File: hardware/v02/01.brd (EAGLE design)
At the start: 91.1 x 43.8 mm, 31 parts, among them IC1 MSP430G2553, IC2 78L05Z, X2 RJ45-6L-B

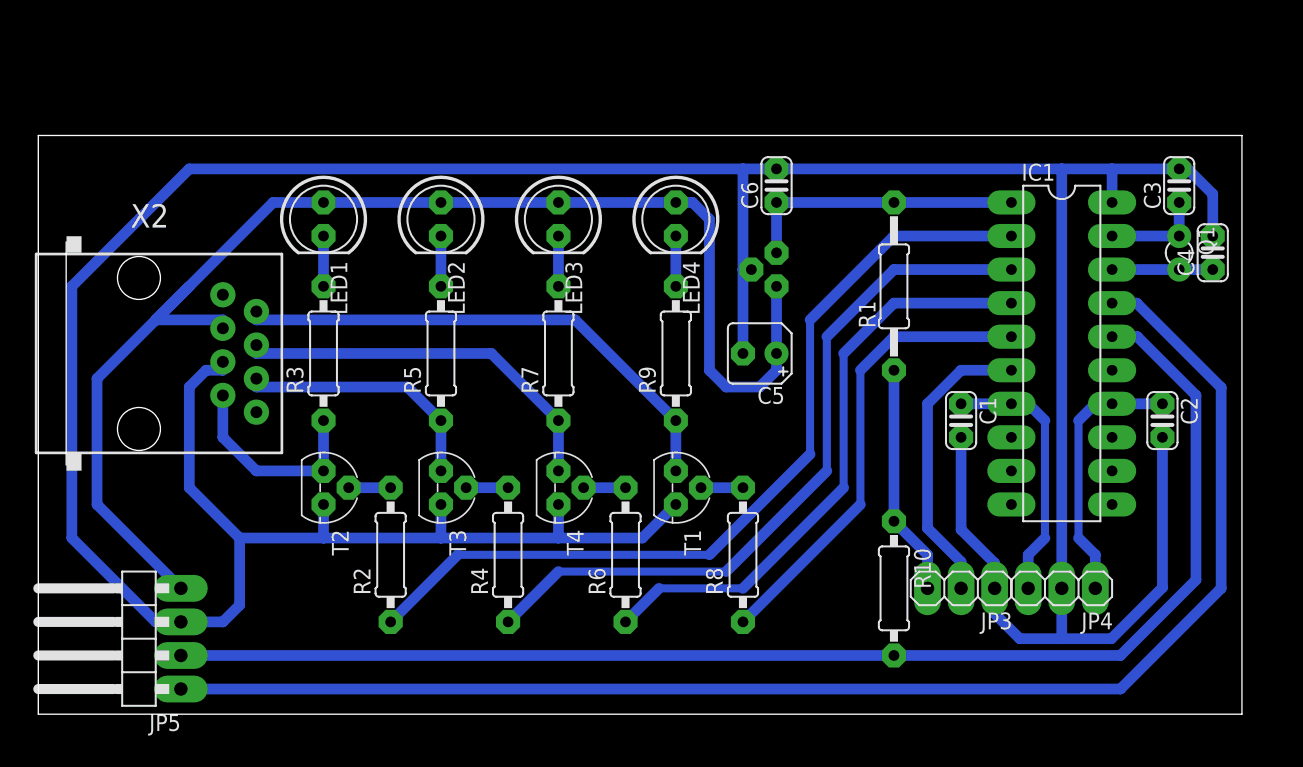
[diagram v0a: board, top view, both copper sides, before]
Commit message: XTAl flat on board; holes for additional wire
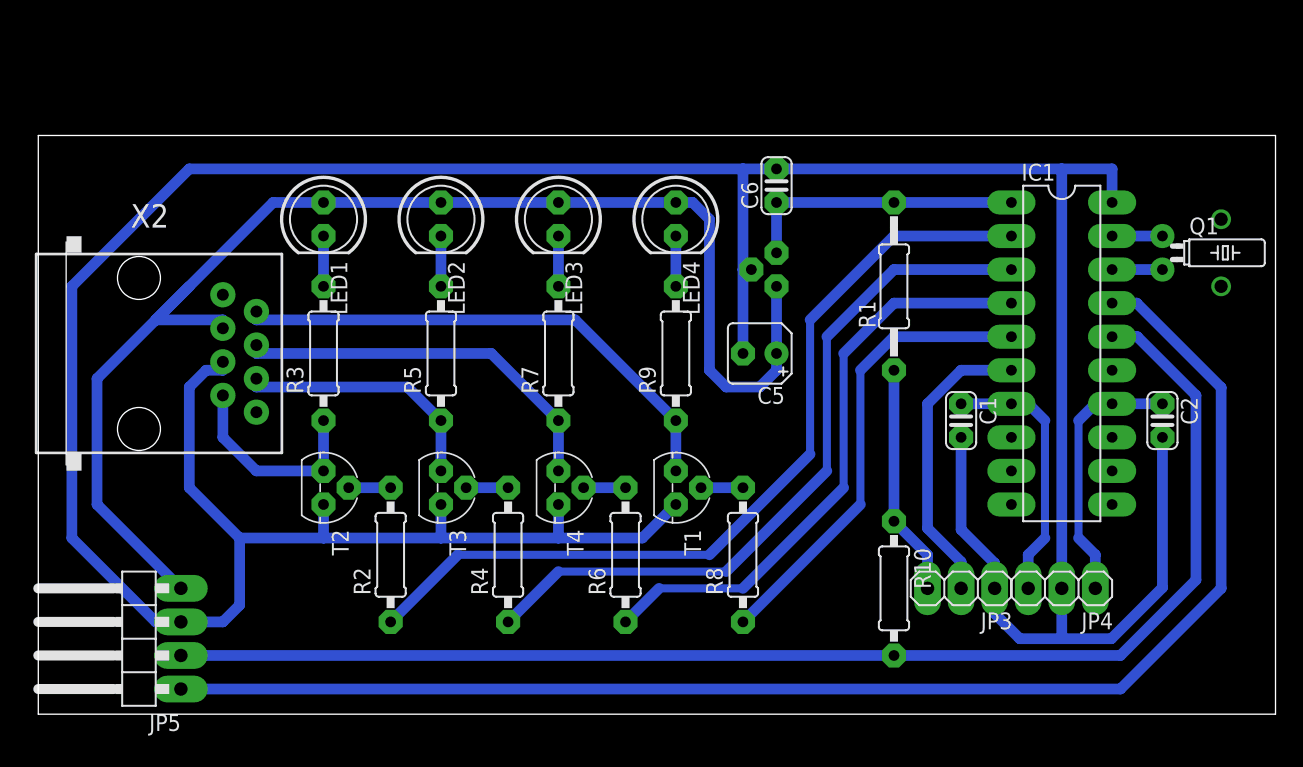
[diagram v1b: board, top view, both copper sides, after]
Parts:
- removed C3, C4: 12pF, rcl:C025-024X044
- Q1: device crystal:TC26V -> crystal:TC26H
- moved Q1 1.27 mm to (85.1, 34.9)
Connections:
- net GND: no longer C3.2, C4.2
- net N$2: no longer C3.1
- net N$7: no longer C4.1
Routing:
- net GND: track 286.0 -> 274.4 mm
- net N$7: track 7.62 -> 3.81 mm
- net N$2: track 7.62 -> 3.81 mm
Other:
- board size 91.1 x 43.8 mm -> 93.7 x 43.8 mm
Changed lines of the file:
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@@
 <board>
 <plain>
-<wire x1="0" y1="0" x2="91.11" y2="0" width="0" layer="20"/>
-<wire x1="91.11" y1="0" x2="91.11" y2="43.805" width="0" layer="20"/>
-<wire x1="91.11" y1="43.805" x2="0" y2="43.805" width="0" layer="20"/>
+<wire x1="0" y1="0" x2="93.65" y2="0" width="0" layer="20"/>
+<wire x1="93.65" y1="0" x2="93.65" y2="43.805" width="0" layer="20"/>
+<wire x1="93.65" y1="43.805" x2="0" y2="43.805" width="0" layer="20"/>
 <wire x1="0" y1="43.805" x2="0" y2="0" width="0" layer="20"/>
 </plain>
@@
 <element name="C1" library="rcl" package="C025-024X044" value="100nF" x="69.85" y="22.225" rot="R270"/>
 <element name="C2" library="rcl" package="C025-024X044" value="100nF" x="85.09" y="22.225" rot="R270"/>
-<element name="Q1" library="crystal" package="TC26V" value="" x="86.36" y="34.925" rot="R270">
-<attribute name="MF" value="" x="86.36" y="34.925" size="1.778" layer="27" rot="R270" display="off"/>
-<attribute name="MPN" value="" x="86.36" y="34.925" size="1.778" layer="27" rot="R270" display="off"/>
-<attribute name="OC_FARNELL" value="unknown" x="86.36" y="34.925" size="1.778" layer="27" rot="R270" display="off"/>
-<attribute name="OC_NEWARK" value="unknown" x="86.36" y="34.925" size="1.778" layer="27" rot="R270" display="off"/>
+<element name="Q1" library="crystal" package="TC26H" value="" x="85.09" y="34.925" rot="R270">
+<attribute name="MF" value="" x="85.09" y="34.925" size="1.778" layer="27" rot="R270" display="off"/>
+<attribute name="MPN" value="" x="85.09" y="34.925" size="1.778" layer="27" rot="R270" display="off"/>
+<attribute name="OC_FARNELL" value="unknown" x="85.09" y="34.925" size="1.778" layer="27" rot="R270" display="off"/>
+<attribute name="OC_NEWARK" value="unknown" x="85.09" y="34.925" size="1.778" layer="27" rot="R270" display="off"/>
 </element>
-<element name="C3" library="rcl" package="C025-024X044" value="12pF" x="86.36" y="40.005" rot="R90"/>
 <element name="R8" library="rcl" package="0207/10" value="470" x="53.34" y="12.065" rot="R90"/>
 <element name="R9" library="rcl" package="0207/10" value="220" x="48.26" y="27.305" rot="R90"/>
@@
 <attribute name="OC_NEWARK" value="16R6090" x="7.62" y="27.305" size="1.778" layer="27" rot="R270" display="off"/>
 </element>
-<element name="C4" library="rcl" package="C025-024X044" value="12pF" x="88.9" y="34.925" rot="R90"/>
 <element name="R1" library="rcl" package="0207/12" value="0" x="64.77" y="32.385" rot="R90"/>
 <element name="R10" library="rcl" package="0207/10" value="47k" x="64.77" y="9.525" rot="R270"/>
@@
 <contactref element="C2" pad="2"/>
 <contactref element="IC1" pad="20"/>
-<contactref element="C3" pad="2"/>
 <contactref element="IC2" pad="2"/>
 <contactref element="C5" pad="-"/>
@@
 <contactref element="X2" pad="5"/>
 <contactref element="JP5" pad="3"/>
-<contactref element="C4" pad="2"/>
 <wire x1="21.59" y1="13.335" x2="21.59" y2="15.875" width="0.8128" layer="16"/>
 <wire x1="21.59" y1="13.335" x2="30.48" y2="13.335" width="0.8128" layer="16"/>
@@
 <wire x1="8.89" y1="6.985" x2="10.795" y2="6.985" width="0.8128" layer="16"/>
 <wire x1="81.28" y1="41.275" x2="81.28" y2="38.735" width="0.8128" layer="16"/>
-<wire x1="81.28" y1="41.275" x2="86.36" y2="41.275" width="0.8128" layer="16"/>
-<wire x1="86.36" y1="41.275" x2="86.995" y2="41.275" width="0.8128" layer="16"/>
-<wire x1="86.995" y1="41.275" x2="88.9" y2="39.37" width="0.8128" layer="16"/>
-<wire x1="88.9" y1="39.37" x2="88.9" y2="36.195" width="0.8128" layer="16"/>
 <wire x1="53.34" y1="33.655" x2="53.975" y2="33.655" width="0.8128" layer="16"/>
 <wire x1="53.34" y1="41.275" x2="53.34" y2="33.655" width="0.8128" layer="16"/>
@@
 </signal>
 <signal name="N$2">
-<contactref element="C3" pad="1"/>
 <contactref element="Q1" pad="1"/>
 <contactref element="IC1" pad="19"/>
-<wire x1="81.28" y1="36.195" x2="86.36" y2="36.195" width="0.8128" layer="16"/>
-<wire x1="86.36" y1="36.195" x2="86.36" y2="38.735" width="0.8128" layer="16"/>
+<wire x1="81.28" y1="36.195" x2="85.09" y2="36.195" width="0.8128" layer="16"/>
 </signal>
 <signal name="N$7">
 <contactref element="Q1" pad="2"/>
 <contactref element="IC1" pad="18"/>
-<contactref element="C4" pad="1"/>
-<wire x1="81.28" y1="33.655" x2="86.36" y2="33.655" width="0.8128" layer="16"/>
-<wire x1="86.36" y1="33.655" x2="88.9" y2="33.655" width="0.8128" layer="16"/>
+<wire x1="81.28" y1="33.655" x2="85.09" y2="33.655" width="0.8128" layer="16"/>
 </signal>
 <signal name="+5V">
@@
 <wire x1="67.31" y1="12.065" x2="67.31" y2="9.525" width="0.8128" layer="16"/>
 </signal>
+<signal name="N$18">
+<via x="89.535" y="37.465" extent="1-16" drill="1" shape="square"/>
+</signal>
+<signal name="N$24">
+<via x="89.535" y="32.385" extent="1-16" drill="1" shape="square"/>
+</signal>
+<signal name="N$25">
+</signal>
+<signal name="N$26">
+</signal>
 </signals>

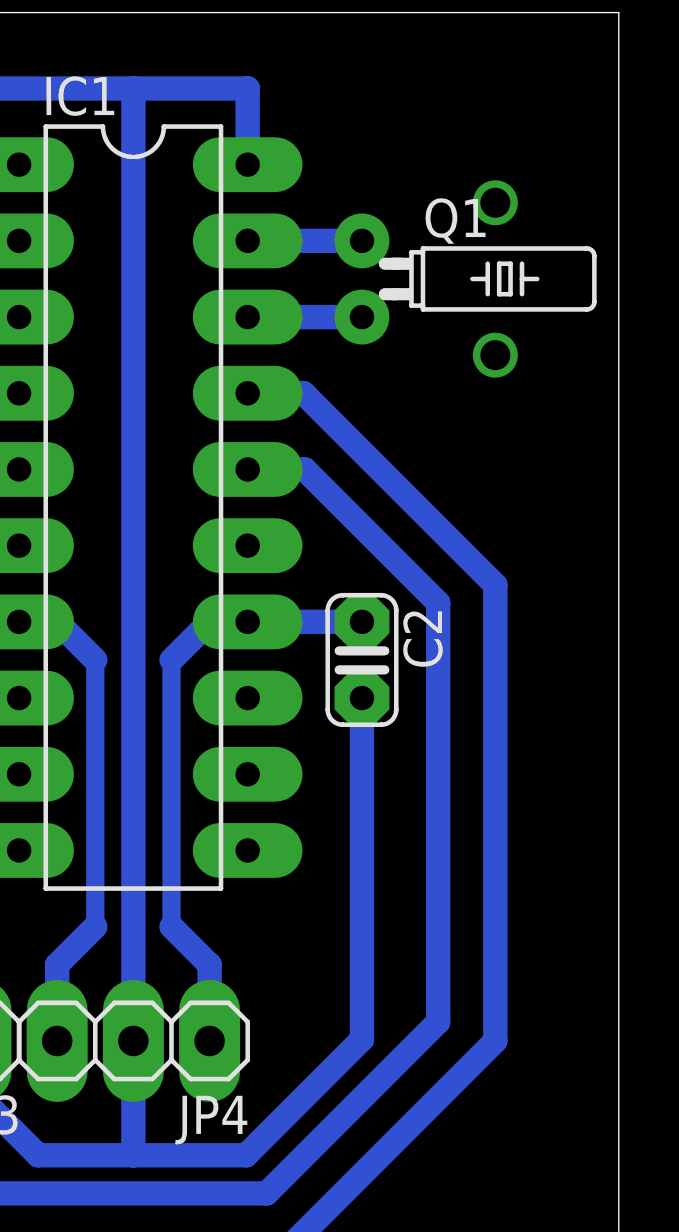
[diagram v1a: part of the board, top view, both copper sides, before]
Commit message: C3 between RST and GND
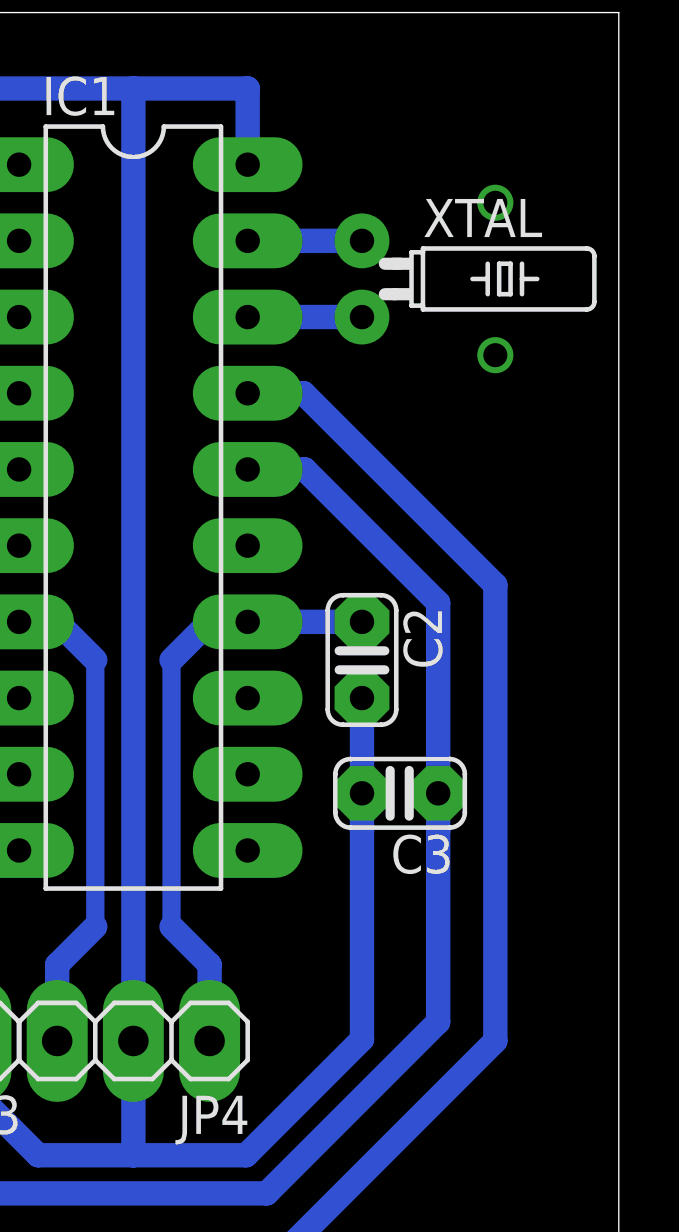
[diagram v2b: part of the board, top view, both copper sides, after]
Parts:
- added C3: 100nF, rcl:C025-024X044
- renumbered Q1 to XTAL
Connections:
- net GND: now also C3.2
- net N$5: now also C3.1
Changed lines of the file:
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@@
 <element name="C1" library="rcl" package="C025-024X044" value="100nF" x="69.85" y="22.225" rot="R270"/>
 <element name="C2" library="rcl" package="C025-024X044" value="100nF" x="85.09" y="22.225" rot="R270"/>
-<element name="Q1" library="crystal" package="TC26H" value="" x="85.09" y="34.925" rot="R270">
+<element name="XTAL" library="crystal" package="TC26H" value="" x="85.09" y="34.925" rot="R270">
 <attribute name="MF" value="" x="85.09" y="34.925" size="1.778" layer="27" rot="R270" display="off"/>
 <attribute name="MPN" value="" x="85.09" y="34.925" size="1.778" layer="27" rot="R270" display="off"/>
@@
 <element name="R1" library="rcl" package="0207/12" value="0" x="64.77" y="32.385" rot="R90"/>
 <element name="R10" library="rcl" package="0207/10" value="47k" x="64.77" y="9.525" rot="R270"/>
+<element name="C3" library="rcl" package="C025-024X044" value="100nF" x="86.36" y="17.78" rot="R180"/>
 </elements>
 <signals>
@@
 <wire x1="77.47" y1="5.715" x2="81.2275" y2="5.715" width="0.8128" layer="16"/>
 <wire x1="81.2275" y1="5.715" x2="85.09" y2="9.5775" width="0.8128" layer="16"/>
-<wire x1="85.09" y1="9.5775" x2="85.09" y2="20.955" width="0.8128" layer="16"/>
+<wire x1="85.09" y1="9.5775" x2="85.09" y2="16.51" width="0.8128" layer="16"/>
+<wire x1="85.09" y1="17.78" x2="85.09" y2="20.955" width="0.8128" layer="16"/>
 <wire x1="53.34" y1="41.275" x2="55.88" y2="41.275" width="0.8128" layer="16"/>
+<contactref element="C3" pad="2"/>
+<wire x1="85.09" y1="17.78" x2="85.09" y2="16.51" width="0.8128" layer="16"/>
 </signal>
 <signal name="N$3">
@@
 <wire x1="64.77" y1="4.445" x2="81.915" y2="4.445" width="0.8128" layer="16"/>
 <wire x1="81.915" y1="4.445" x2="87.63" y2="10.16" width="0.8128" layer="16"/>
-<wire x1="87.63" y1="10.16" x2="87.63" y2="24.13" width="0.8128" layer="16"/>
+<wire x1="87.63" y1="10.16" x2="87.63" y2="16.51" width="0.8128" layer="16"/>
+<wire x1="87.63" y1="17.78" x2="87.63" y2="24.13" width="0.8128" layer="16"/>
 <wire x1="87.63" y1="24.13" x2="83.185" y2="28.575" width="0.8128" layer="16"/>
 <wire x1="83.185" y1="28.575" x2="81.28" y2="28.575" width="0.8128" layer="16"/>
 <contactref element="R10" pad="2"/>
+<contactref element="C3" pad="1"/>
+<wire x1="87.63" y1="17.78" x2="87.63" y2="16.51" width="0.8128" layer="16"/>
 </signal>
 <signal name="N$6">
@@
 </signal>
 <signal name="N$2">
-<contactref element="Q1" pad="1"/>
+<contactref element="XTAL" pad="1"/>
 <contactref element="IC1" pad="19"/>
 <wire x1="81.28" y1="36.195" x2="85.09" y2="36.195" width="0.8128" layer="16"/>
 </signal>
 <signal name="N$7">
-<contactref element="Q1" pad="2"/>
+<contactref element="XTAL" pad="2"/>
 <contactref element="IC1" pad="18"/>
 <wire x1="81.28" y1="33.655" x2="85.09" y2="33.655" width="0.8128" layer="16"/>
@@
 </signal>
 <signal name="N$18">
-<via x="89.535" y="37.465" extent="1-16" drill="1" shape="square"/>
+<via x="89.535" y="37.465" extent="1-16" drill="0.8"/>
 </signal>
 <signal name="N$24">
-<via x="89.535" y="32.385" extent="1-16" drill="1" shape="square"/>
+<via x="89.535" y="32.385" extent="1-16" drill="0.8"/>
 </signal>
 <signal name="N$25">

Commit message: C4 between Vcc and GND
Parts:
- removed C6: 100nF, rcl:C025-024X044
- added C4: 200nF, rcl:B45181A
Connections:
- net GND: now also C4.-; no longer C6.2
- net VCC: now also C4.+; no longer C6.1
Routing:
- net GND: track 274.4 -> 287.7 mm
- net VCC: track 21.6 -> 22.9 mm
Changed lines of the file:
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@@
 <element name="JP4" library="pinhead" package="1X03" value="" x="77.47" y="9.525" rot="R180"/>
 <element name="JP5" library="pinhead" package="1X04/90" value="" x="6.985" y="5.715" rot="R90"/>
-<element name="C6" library="rcl" package="C025-024X044" value="100nF" x="55.88" y="40.005" rot="R90"/>
 <element name="X2" library="con-tycoelectronics" package="RJ45-NO-SHIELD" value="RJ45-6L-B" x="7.62" y="27.305" rot="R270">
 <attribute name="MF" value="" x="7.62" y="27.305" size="1.778" layer="27" rot="R270" display="off"/>
@@
 <element name="R10" library="rcl" package="0207/10" value="47k" x="64.77" y="9.525" rot="R270"/>
 <element name="C3" library="rcl" package="C025-024X044" value="100nF" x="86.36" y="17.78" rot="R180"/>
+<element name="C4" library="rcl" package="B45181A" value="200nF" x="54.61" y="40.005" rot="R180"/>
 </elements>
 <signals>
@@
 <contactref element="IC1" pad="1"/>
 <contactref element="IC2" pad="1"/>
-<contactref element="C6" pad="1"/>
 <contactref element="R1" pad="2"/>
 <wire x1="64.77" y1="38.735" x2="73.66" y2="38.735" width="0.8128" layer="16"/>
-<wire x1="55.88" y1="34.925" x2="55.88" y2="38.735" width="0.8128" layer="16"/>
-<wire x1="55.88" y1="38.735" x2="64.77" y2="38.735" width="0.8128" layer="16"/>
+<contactref element="C4" pad="+"/>
+<wire x1="55.88" y1="40.005" x2="55.88" y2="38.735" width="0.8128" layer="16"/>
+<wire x1="55.88" y1="38.735" x2="55.88" y2="34.925" width="0.8128" layer="16"/>
+<wire x1="64.77" y1="38.735" x2="55.88" y2="38.735" width="0.8128" layer="16"/>
 </signal>
 <signal name="PR">
@@
 <contactref element="JP3" pad="1"/>
 <contactref element="JP4" pad="2"/>
-<contactref element="C6" pad="2"/>
 <contactref element="X2" pad="5"/>
 <contactref element="JP5" pad="3"/>
@@
 <wire x1="13.97" y1="6.985" x2="15.24" y2="8.255" width="0.8128" layer="16"/>
 <wire x1="15.24" y1="8.255" x2="15.24" y2="13.335" width="0.8128" layer="16"/>
-<wire x1="55.88" y1="41.275" x2="77.47" y2="41.275" width="0.8128" layer="16"/>
 <wire x1="77.47" y1="41.275" x2="81.28" y2="41.275" width="0.8128" layer="16"/>
 <wire x1="11.43" y1="41.275" x2="53.34" y2="41.275" width="0.8128" layer="16"/>
@@
 <wire x1="81.28" y1="41.275" x2="81.28" y2="38.735" width="0.8128" layer="16"/>
 <wire x1="53.34" y1="33.655" x2="53.975" y2="33.655" width="0.8128" layer="16"/>
-<wire x1="53.34" y1="41.275" x2="53.34" y2="33.655" width="0.8128" layer="16"/>
+<wire x1="53.34" y1="40.005" x2="53.34" y2="33.655" width="0.8128" layer="16"/>
 <wire x1="53.34" y1="33.655" x2="53.34" y2="27.305" width="0.8128" layer="16"/>
 <wire x1="77.47" y1="41.275" x2="77.47" y2="9.525" width="0.8128" layer="16"/>
@@
 <wire x1="77.47" y1="5.715" x2="81.2275" y2="5.715" width="0.8128" layer="16"/>
 <wire x1="81.2275" y1="5.715" x2="85.09" y2="9.5775" width="0.8128" layer="16"/>
-<wire x1="85.09" y1="9.5775" x2="85.09" y2="16.51" width="0.8128" layer="16"/>
+<wire x1="85.09" y1="9.5775" x2="85.09" y2="17.78" width="0.8128" layer="16"/>
 <wire x1="85.09" y1="17.78" x2="85.09" y2="20.955" width="0.8128" layer="16"/>
-<wire x1="53.34" y1="41.275" x2="55.88" y2="41.275" width="0.8128" layer="16"/>
 <contactref element="C3" pad="2"/>
-<wire x1="85.09" y1="17.78" x2="85.09" y2="16.51" width="0.8128" layer="16"/>
+<contactref element="C4" pad="-"/>
+<wire x1="53.34" y1="40.005" x2="53.34" y2="41.275" width="0.8128" layer="16"/>
+<wire x1="53.34" y1="27.305" x2="53.34" y2="40.64" width="0.8128" layer="16"/>
+<wire x1="53.34" y1="41.275" x2="77.47" y2="41.275" width="0.8128" layer="16"/>
 </signal>
 <signal name="N$3">
